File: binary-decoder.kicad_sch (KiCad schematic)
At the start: 4 parts, among them Q0 Q_NMOS_DGS, Q1 Q_NMOS_DGS, U6 SN74LS08N, U8 SN74HC86N

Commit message: feat: updated references
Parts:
- Q0, Q1: value Q_NMOS_DGS -> DMG2302U-7
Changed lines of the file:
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@@
 			)
 		)
-		(property "Value" "Q_NMOS_DGS"
+		(property "Value" "DMG2302U-7"
 			(at 132.588 105.156 0)
 			(show_name no)
@@
 			)
 		)
-		(property "Value" "Q_NMOS_DGS"
+		(property "Value" "DMG2302U-7"
 			(at 113.538 80.01 0)
 			(show_name no)

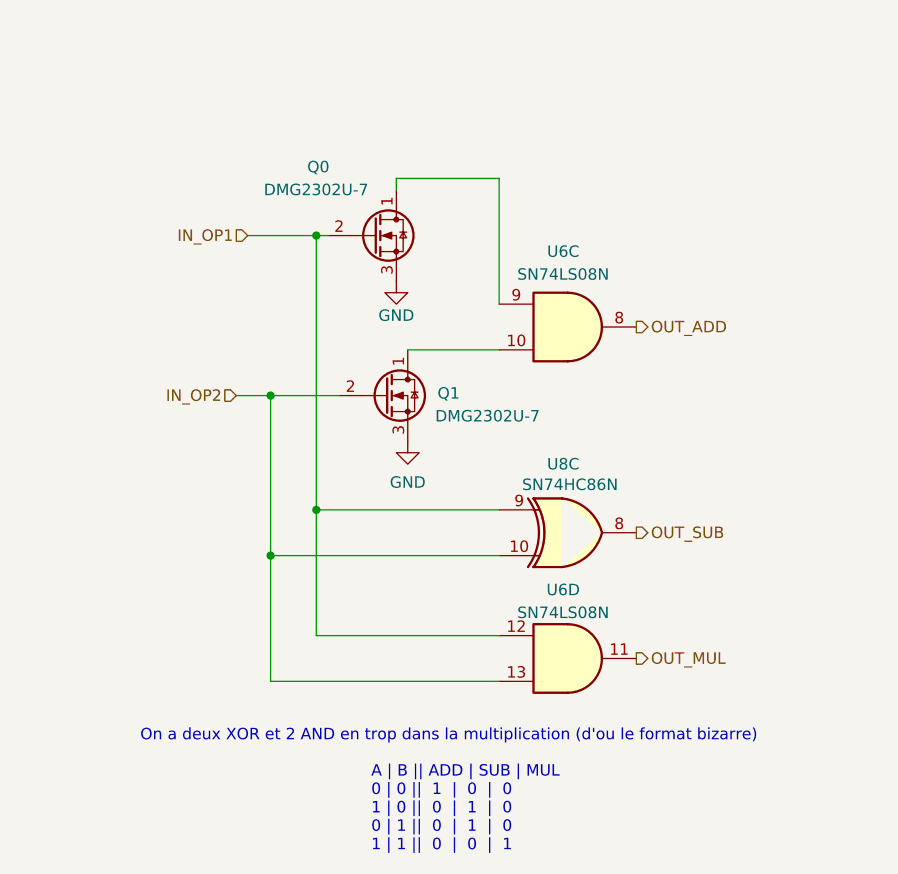
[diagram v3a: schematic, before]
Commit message: feat: missing pull up
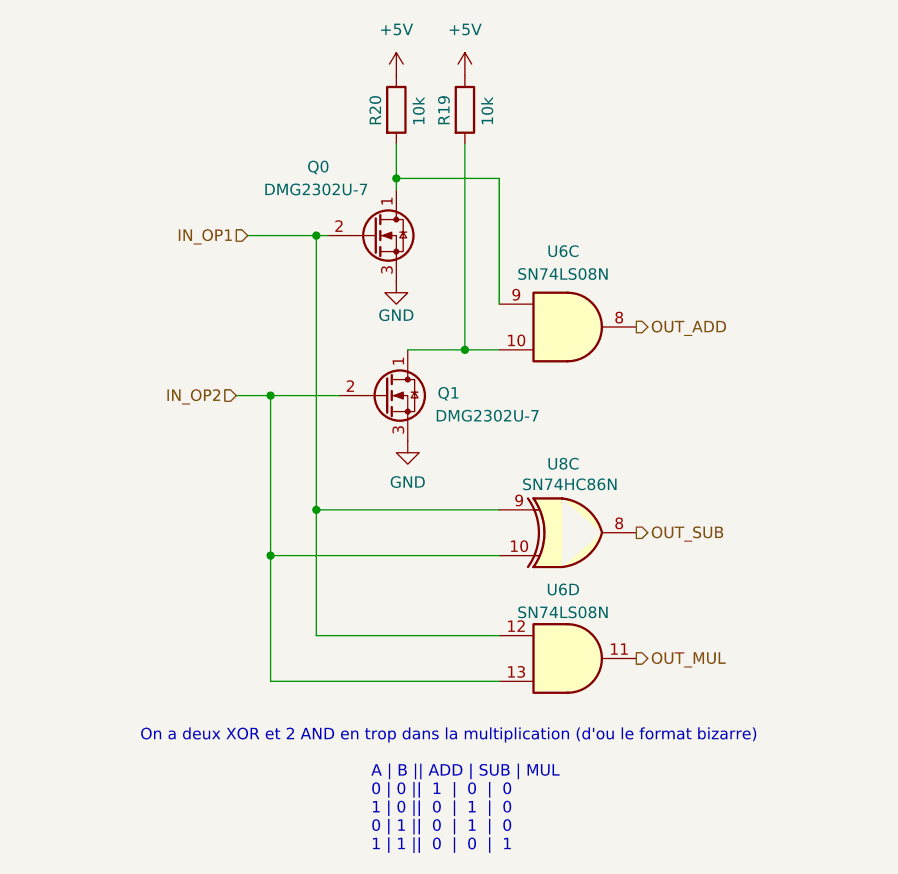
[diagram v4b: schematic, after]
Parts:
- added R19, R20: 10k, Resistor_SMD:R_0603_1608Metric_Pad0.98x0.95mm_HandSolder, symbol Device:R
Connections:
- net at Q1.1 (D), U6.10: now also R19.2
- net at Q0.1 (D), U6.9: now also R20.2
- new net +5V: R19.1, R20.1

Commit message: feat: multiplier schema
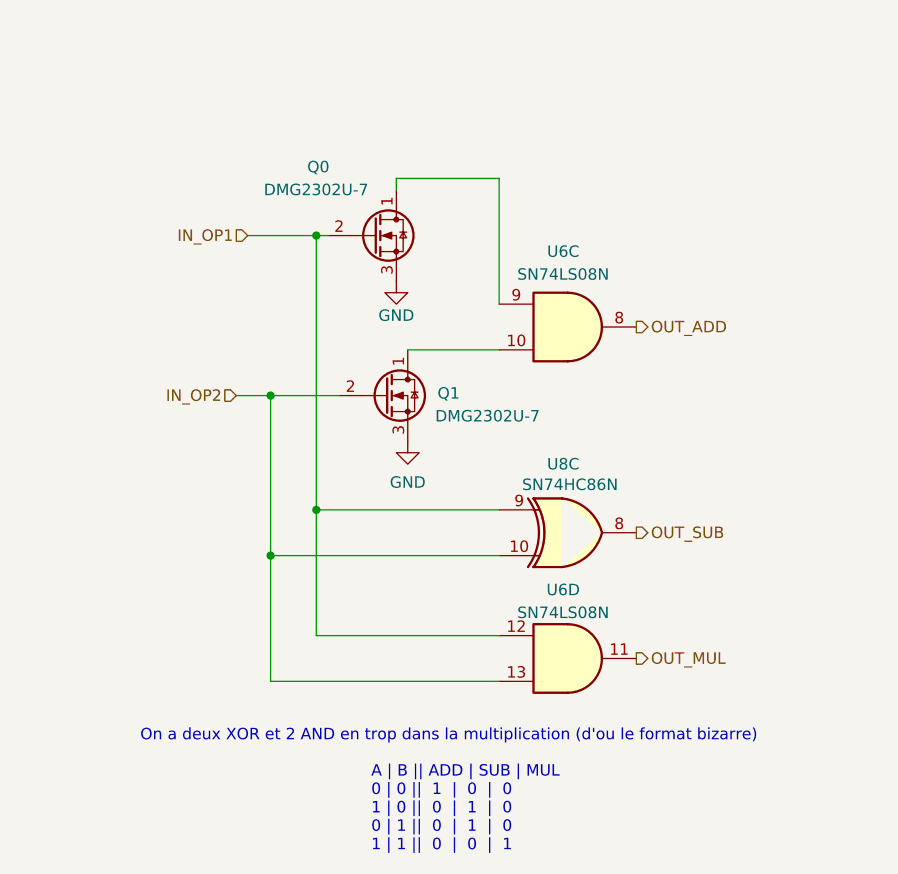
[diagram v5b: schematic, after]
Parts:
- removed R19, R20: 10k, Resistor_SMD:R_0603_1608Metric_Pad0.98x0.95mm_HandSolder, symbol Device:R
